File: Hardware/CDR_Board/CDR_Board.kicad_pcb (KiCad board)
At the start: 2 copper layers, 61 x 40.6 mm, 59 parts, among them J1 nRF52, J2 nRF24, J3 Battery, J4 Conn_01x06, J5 USB_C_Receptacle_USB2.0, Q1 DMP2045U, SW1 BOOTSEL, SW2 RESET, U1 W25Q32JVSS, U2 SOT23-5 200mA 3.3V, U3 RP2040, U4 BQ25172, U6 ADXL343, Y1 Crystal

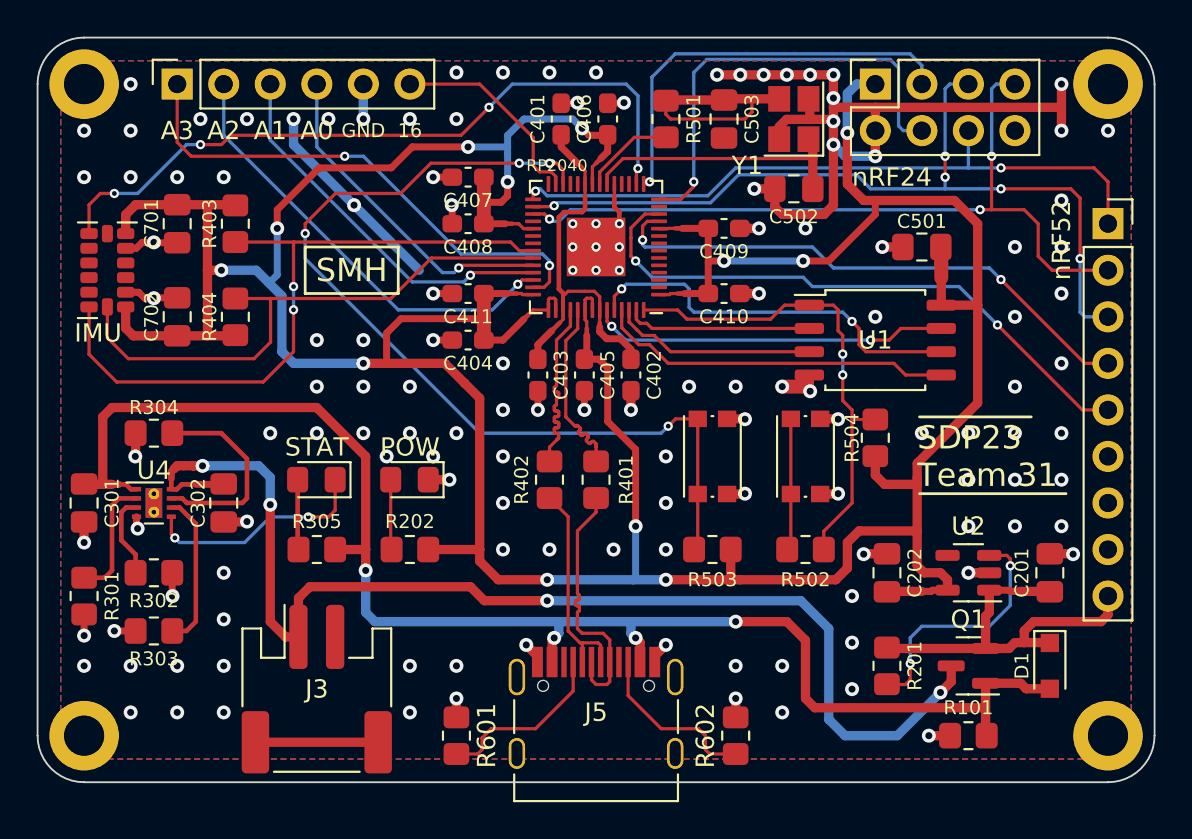
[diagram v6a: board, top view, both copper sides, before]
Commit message: Updated helmet PCB
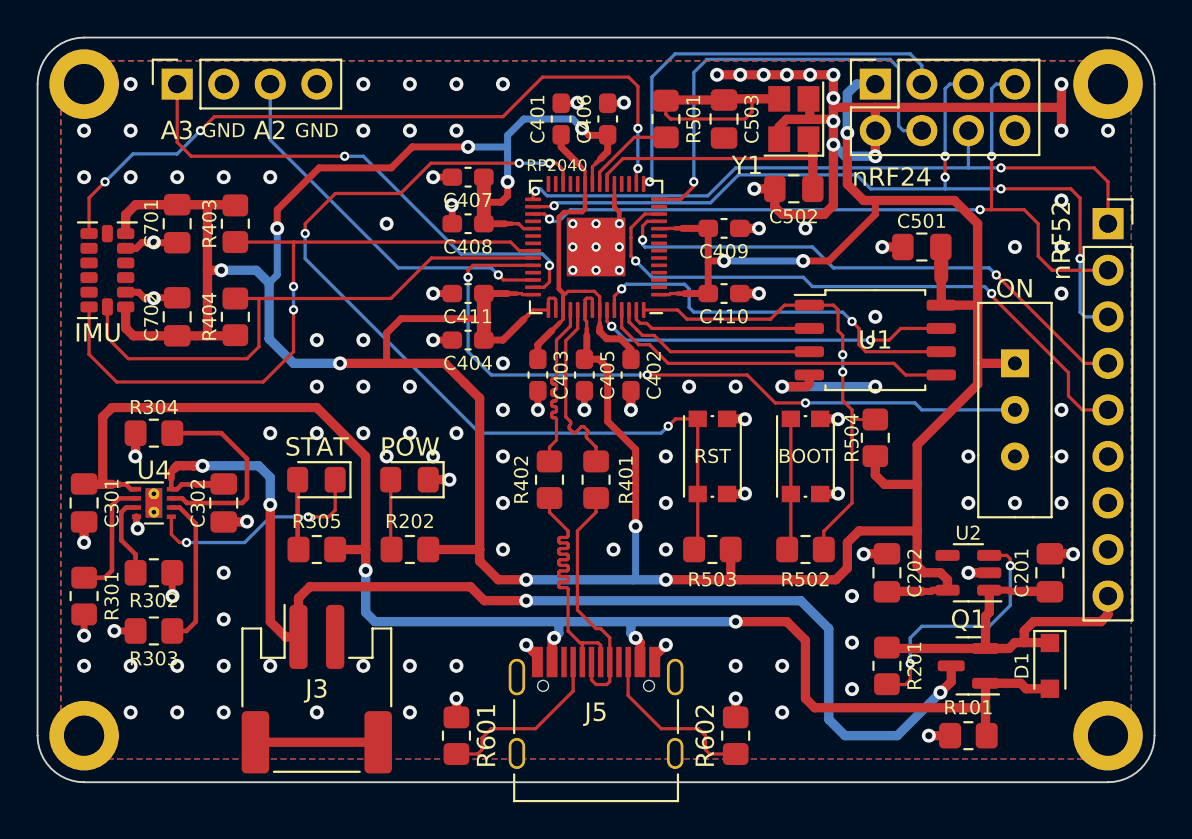
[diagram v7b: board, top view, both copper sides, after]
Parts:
- added SW3: SW_SPDT, SPDT_Footprint:E-Switch-EG1218, F.Cu at (175.3, 94.0)
- C501: value C -> 100n
- J4: value Conn_01x06 -> GPIO & ADC; footprint Connector_PinSocket_2.54mm:PinSocket_1x06_P2.54mm_Vertical -> Connector_PinSocket_2.54mm:PinSocket_1x04_P2.54mm_Vertical
- R501: value 1k -> 4k7
- U2: value SOT23-5 200mA 3.3V -> AP2112
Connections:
- J4 pad 2: /A2 -> GND
- J4 pad 3: /A1 -> /A2
- J4 pad 4: /A0 -> GND
- U3 pad 27: /GPIO16 -> unconnected-(U3-Pad27)
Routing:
- net /A0: track 18.2 -> 39.3 mm, vias 1 -> 3
- net /A1: track 20.8 -> 0.00 mm, vias 1 -> 0
- net /GPIO16: track 11.4 -> 0.00 mm
- net GND: track 103.1 -> 94.7 mm, vias 139 -> 131
- net /D-: track 12.0 -> 16.3 mm
- net /A2: track 24.3 -> 20.6 mm
- net +3V3: track 224.2 -> 226.2 mm
- net /D+: track 14.2 -> 13.2 mm
- net /D13: track 39.4 -> 40.2 mm
- net /BLE_IRQ: track 32.9 -> 33.7 mm
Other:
- board text added: "BOOT"
- board text added: "ON"
- board text added: "RST"
- board text removed: "16"
- board text removed: "A0"
- board text removed: "A1"
- board text removed: "SDP23 Team 31"
- board text removed: "SMH"
